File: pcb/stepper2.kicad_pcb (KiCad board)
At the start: 2 copper layers, 91.5 x 138 mm, 49 parts, among them J1 DA15_Receptacle_MountingHoles, J10 Conn_01x07_Pin, J2 DA15_Receptacle_MountingHoles, J3 DA15_Receptacle_MountingHoles, J4 DE15_Receptacle_HighDensity, J5 DE15_Receptacle_HighDensity, J6 DE15_Receptacle_HighDensity, J7 Conn_01x04_Pin, J8 Conn_01x05_Pin, J9 Conn_01x06_Pin, SW1 SW_Push, SW2 SW_Push, SW3 SW_Push, SW4 SW_Push, SW5 SW_Push, SW6 SW_Push, U1 AM26LS32ACN, U2 AM26LS32Ax, U3 AM26LS32ACN, U4 TMC2209_BIGTREETECH, U5 TMC2209_BIGTREETECH, U6 TMC2209_BIGTREETECH

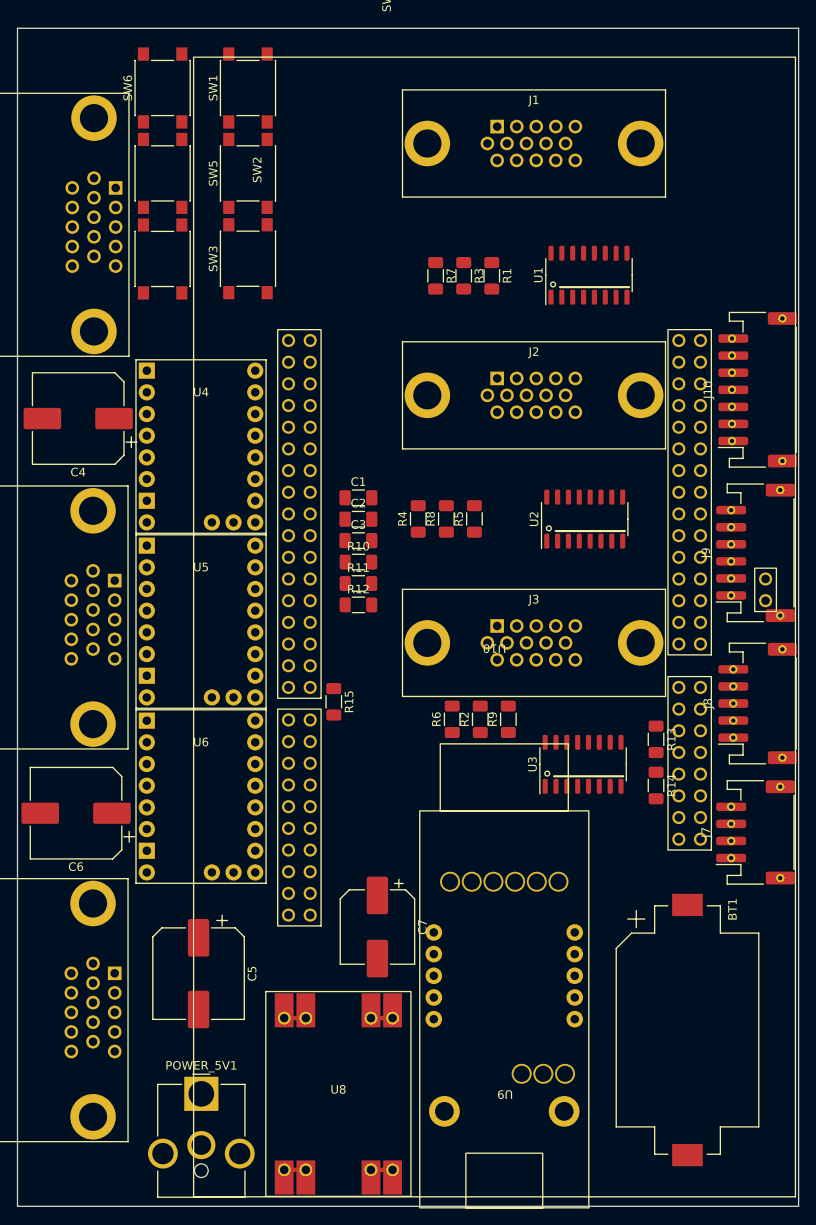
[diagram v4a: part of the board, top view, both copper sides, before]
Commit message: tweaks in PCB and fixed rotated nucleo parts in schematic
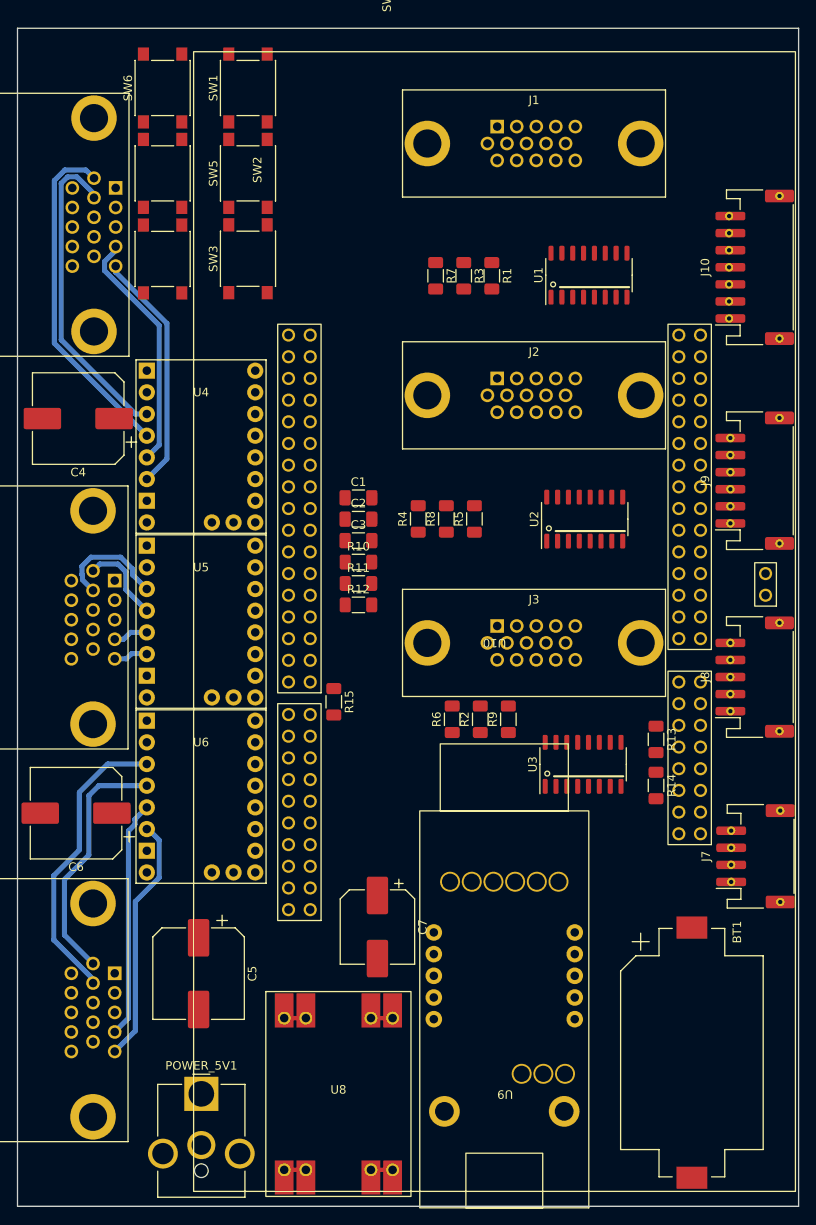
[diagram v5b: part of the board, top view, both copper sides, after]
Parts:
- moved J10 14.4 mm to (86.4, 28.0)
- moved J9 8.45 mm to (86.4, 53.0)
- moved J8 3.12 mm to (86.4, 76.0)
- moved J7 2.80 mm to (86.5, 97.0)
- moved BT1 2.70 mm to (79.0, 120.0)
- moved U10 0.64 mm to (55.9, 71.5)
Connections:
- J4 pad 7: MYA1 -> MXB1
- J5 pad 7: MYA2 -> MXB2
- J6 pad 7: MYA3 -> MXB3
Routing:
- net MXA1: track 0.00 -> 39.9 mm
- net MXB1: track 0.00 -> 37.4 mm
- net MXB3: track 0.00 -> 34.8 mm
- net MXA3: track 0.00 -> 29.5 mm
- net MYB3: track 0.00 -> 28.9 mm
- net MYA1: track 0.00 -> 28.5 mm
- net MYB1: track 0.00 -> 28.4 mm
- net MYA3: track 0.00 -> 27.9 mm
- net MXB2: track 0.00 -> 13.3 mm
- net MXA2: track 0.00 -> 10.1 mm
- net MYA2: track 0.00 -> 4.10 mm
- net MYB2: track 0.00 -> 4.04 mm
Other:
- copper layers 2 -> 4

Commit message: DIR and EN pins connected to GPIO
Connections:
- U10 pad A10: EXTSDA -> TMCUARTTX2
- U10 pad A11: EXTCOPI -> GND
- U10 pad A12: EXTSCL -> TMCUART2
- U10 pad A13: EXTCIPO -> GND
- U10 pad A15: EXTCS -> unconnected-(U10A-VIN-PadA15)
- U10 pad A17: EXTCLK -> unconnected-(U10A-PA3-PadA17)
- U10 pad A19: GND -> unconnected-(U10A-PC0-PadA19)
- U10 pad A2: TMCUART1 -> DIR3
- U10 pad A20: unconnected-(U10A-PD6-PadA20) -> USBUARTRX
- U10 pad A22: unconnected-(U10A-PD5-PadA22) -> USBUARTTX
- U10 pad A25: USBUARTTX -> unconnected-(U10A-PC2-PadA25)
- U10 pad A27: USBUARTRX -> unconnected-(U10A-PF10-PadA27)
- U10 pad A28: unconnected-(U10A-GND-PadA28) -> GND
- U10 pad A3: EXTA2 -> unconnected-(U10A-IOREF-PadA3)
- U10 pad A30: unconnected-(U10A-PE2-PadA30) -> EXTCLK
- U10 pad A32: unconnected-(U10A-PE4-PadA32) -> EXTCS
- U10 pad A34: GND -> EXTCIPO
- U10 pad A35: TMCUART2 -> EXTSCL
- U10 pad A36: GND -> EXTCOPI
- U10 pad A37: TMCUARTTX2 -> EXTSDA
- U10 pad A38: +5V -> unconnected-(U10A-PE3-PadA38)
- U10 pad A39: TMCUART3 -> GND
- U10 pad A40: +3V3 -> EXTA1
- U10 pad A41: TMCUARTTX3 -> unconnected-(U10A-PD0-PadA41)
- U10 pad A42: unconnected-(U10A-PF7-PadA42) -> EXTTX
- U10 pad A44: unconnected-(U10A-PF9-PadA44) -> EXTA2
- U10 pad A45: unconnected-(U10A-PG0-PadA45) -> TMCUART1
- U10 pad A5: EXTTX -> unconnected-(U10A-NRST-PadA5)
- U10 pad A6: unconnected-(U10A-PC10-PadA6) -> TMCUARTTX3
- U10 pad A7: EXTA1 -> +3V3
- U10 pad A8: GND -> TMCUART3
- U10 pad A9: unconnected-(U10A-5V-PadA9) -> +5V
- U10 pad B1: unconnected-(U10B-PC6-PadB1) -> ENCA3
- U10 pad B10: unconnected-(U10B-PA5-PadB10) -> EXTDAC2
- U10 pad B11: unconnected-(U10B-PC7-PadB11) -> ENCB3
- U10 pad B12: ENCI1 -> ENCA2
- U10 pad B13: GND -> unconnected-(U10B-PB5-PadB13)
- U10 pad B14: ENCA1 -> ENCB2
- U10 pad B16: ENCB1 -> ENCI2
- U10 pad B17: unconnected-(U10B-PA4-PadB17) -> EXTDAC1
- U10 pad B18: GND -> TMCUARTTX1
- U10 pad B19: DIAG1 -> unconnected-(U10B-PB4-PadB19)
- U10 pad B2: unconnected-(U10B-PB8-PadB2) -> DIAG3
- U10 pad B20: unconnected-(U10B-PF3-PadB20) -> EN3
- U10 pad B21: DIAG2 -> unconnected-(U10B-AVDD-PadB21)
- U10 pad B22: unconnected-(U10B-PG12-PadB22) -> NXT2
- U10 pad B23: unconnected-(U10B-GND-PadB23) -> GND
- U10 pad B24: EXTRX -> VREFPWM1
- U10 pad B25: VREFPWM3 -> GND
- U10 pad B26: unconnected-(U10B-PE11-PadB26) -> VREFPWM2
- U10 pad B27: unconnected-(U10B-PF4-PadB27) -> DIR2
- U10 pad B28: unconnected-(U10B-PE14-PadB28) -> RLIMIT2
- U10 pad B29: VREFPWM2 -> EN2
- U10 pad B3: unconnected-(U10B-PB15-PadB3) -> ENCI3
- U10 pad B30: GND -> VREFPWM3
- U10 pad B31: VREFPWM1 -> EXTRX
- U10 pad B32: GND -> FLIMIT2
- U10 pad B33: NXT2 -> DIR1
- U10 pad B34: unconnected-(U10B-PB6-PadB34) -> DIAG2
- U10 pad B35: unconnected-(U10B-PB2-PadB35) -> EN1
- U10 pad B36: unconnected-(U10B-PB7-PadB36) -> DIAG1
- U10 pad B37: TMCUARTTX1 -> GND
- U10 pad B38: EXTDAC1 -> RLIMIT1
- U10 pad B39: ENCI2 -> ENCB1
- U10 pad B4: unconnected-(U10B-PB9-PadB4) -> RLIMIT3
- U10 pad B40: unconnected-(U10B-PE7-PadB40) -> FLIMIT1
- U10 pad B41: ENCB2 -> ENCA1
- U10 pad B42: unconnected-(U10B-GND-PadB42) -> GND
- U10 pad B43: ENCA2 -> ENCI1
- U10 pad B44: ENCB3 -> UP3
- U10 pad B45: EXTDAC2 -> unconnected-(U10B-PE2-PadB45)
- U10 pad B46: unconnected-(U10B-PE12-PadB46) -> UP2
- U10 pad B49: unconnected-(U10B-PA0-PadB49) -> NXT1
- U10 pad B50: unconnected-(U10B-PE15-PadB50) -> DOWN3
- U10 pad B51: NXT3 -> unconnected-(U10B-PB0-PadB51)
- U10 pad B52: ENCI3 -> DOWN2
- U10 pad B53: DIAG3 -> UP1
- U10 pad B54: ENCA3 -> DOWN1
- U10 pad B6: NXT1 -> unconnected-(U10B-VREFP-PadB6)
- U10 pad B7: unconnected-(U10B-PB12-PadB7) -> FLIMIT3
- U10 pad B9: unconnected-(U10B-PA15-PadB9) -> NXT3

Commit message: First complete version of the PCB
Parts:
- added H1: MountingHole, stepper2:MountingHole_3.2mm_M3, F.Cu at (5.00, 133.0)
- added H2: MountingHole, stepper2:MountingHole_3.2mm_M3, F.Cu at (5.00, 5.00)
- added J11: FAN, Connector_JST:JST_XH_B2B-XH-AM_1x02_P2.50mm_Vertical, F.Cu at (42.9, 99.0)
- C1, C2, C3: value 2u2 -> 22u
- C4, C5, C6: value C_Polarized -> 24V
- C7: value C_Polarized -> 5V
- moved J7 85.5 mm to (86.5, 11.5)
- moved J10 51.0 mm to (86.6, 79.0)
- moved C7 44.6 mm to (86.5, 100.0)
- moved U8 44.6 mm to (82.2, 125.1)
- moved J8 44.0 mm to (86.5, 32.0)
- moved BT1 39.0 mm to (40.0, 121.7)
- moved C3 37.1 mm to (24.0, 93.5), turned to 180 degrees
- moved R12 32.6 mm to (24.0, 96.0), turned to 180 degrees
- moved R15 26.4 mm to (37.0, 52.5)
- moved R4 25.1 mm to (71.5, 52.0)
- moved R7 23.4 mm to (71.5, 22.5), turned to 90 degrees
- moved C2 21.9 mm to (24.0, 72.5), turned to 180 degrees
- moved R11 19.1 mm to (24.0, 75.5), turned to 180 degrees
- moved R8 18.1 mm to (67.5, 52.0)
- moved R10 17.6 mm to (24.0, 55.0), turned to 180 degrees
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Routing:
- net +3V3: track 0.00 -> 157.6 mm
- net VBAT: track 0.00 -> 83.1 mm, vias 0 -> 3
- net EXTDAC2: track 0.00 -> 75.8 mm
- net DIR3: track 0.00 -> 64.0 mm, vias 0 -> 1
- net TMCUART1: track 0.00 -> 63.8 mm, vias 0 -> 1
- net EXTRX: track 0.00 -> 63.8 mm
- net TMCUART2: track 0.00 -> 60.0 mm, vias 0 -> 1
- net VCC: track 0.00 -> 57.9 mm, vias 0 -> 12
- net DOWN3: track 0.00 -> 56.2 mm
- net TMCUART3: track 0.00 -> 53.5 mm, vias 0 -> 1
- net EXTDAC1: track 0.00 -> 53.4 mm, vias 0 -> 1
- net ENCB2: track 0.00 -> 50.9 mm
- net USBUARTTX: track 0.00 -> 50.7 mm
- net ENCI2: track 0.00 -> 50.0 mm
- net ENCA2: track 0.00 -> 49.4 mm
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- added copper zone on In2.Cu, net +3V3
- added copper zone on In2.Cu, net +5V
- added copper zone on B.Cu, net GND
- added copper zone on F.Cu, net GND
- added copper zone on In1.Cu, net GND
- added copper zone on In2.Cu, net VCC
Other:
- board size 91.5 x 138 mm -> 92 x 138 mm
- board text added: "Nucleo: move 5V PWR jumper to EXT Nucleo: remove SB52 to use 3V battery Remove jumper from USB-UART converter"

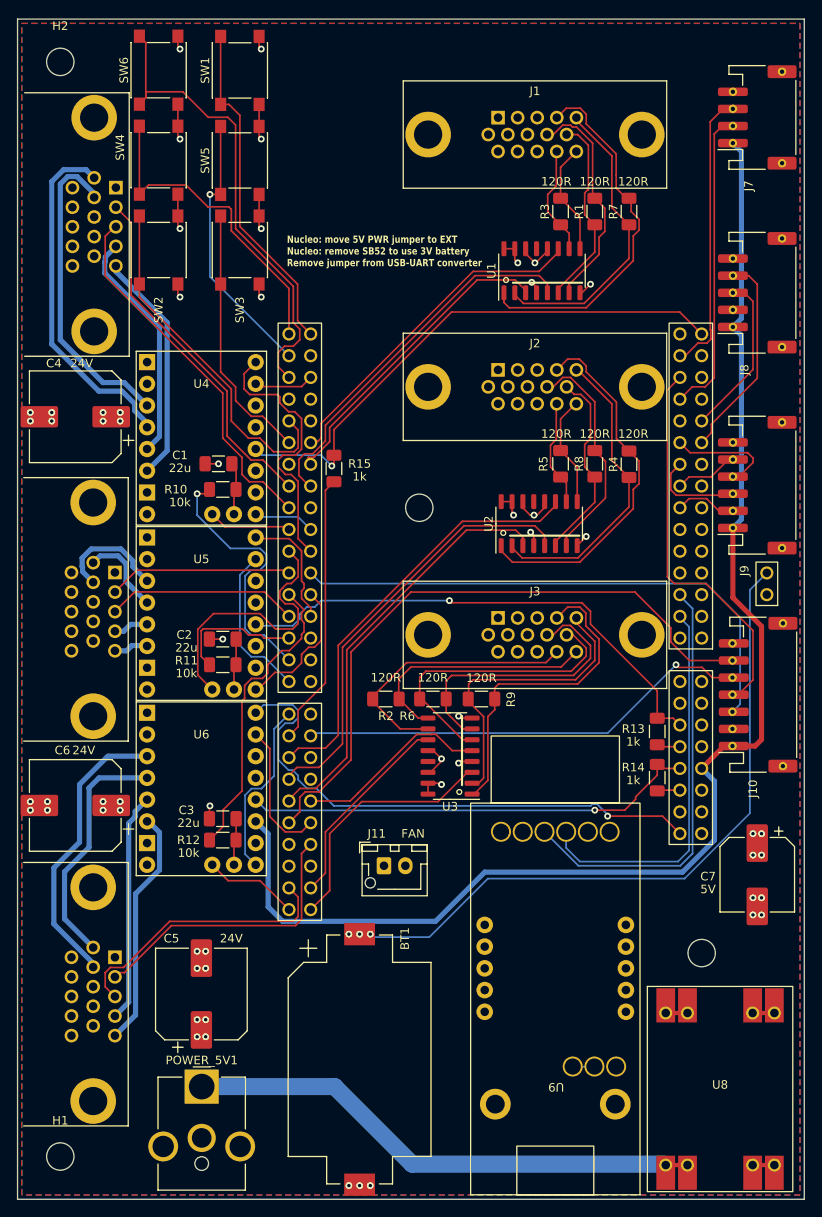
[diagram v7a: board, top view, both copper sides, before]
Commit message: Revert to 2 layer PCB
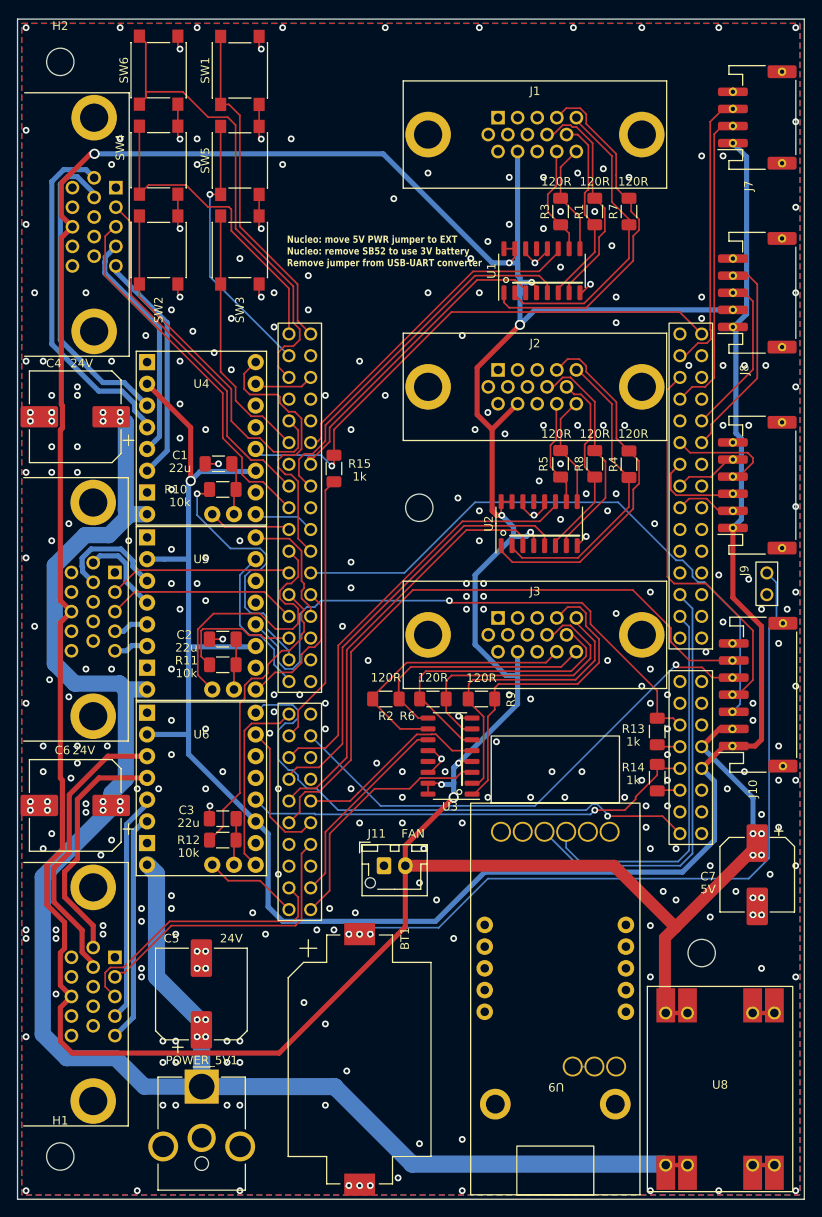
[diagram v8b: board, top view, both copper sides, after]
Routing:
- net +5V: track 13.7 -> 456.3 mm, vias 10 -> 13
- net VCC: track 57.9 -> 204.3 mm
- net +3V3: track 157.6 -> 240.5 mm, vias 0 -> 1
- net TMCUART2: track 60.0 -> 68.2 mm
- net EXTRX: track 63.8 -> 71.1 mm
- net EXTDAC1: track 53.4 -> 60.2 mm
- net VBAT: track 83.1 -> 88.4 mm
- net GND: track 48.5 -> 43.4 mm, vias 36 -> 307
- net EN3: track 20.9 -> 22.2 mm
- net MYB3: track 27.9 -> 26.8 mm
- removed copper zone on In2.Cu, net +3V3
- removed copper zone on In2.Cu, net +5V
- removed copper zone on In1.Cu, net GND
- removed copper zone on In2.Cu, net VCC
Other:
- copper layers 4 -> 2
